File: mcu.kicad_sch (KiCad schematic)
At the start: 1 part, among them U1 XU316-1024-QF60A-C32

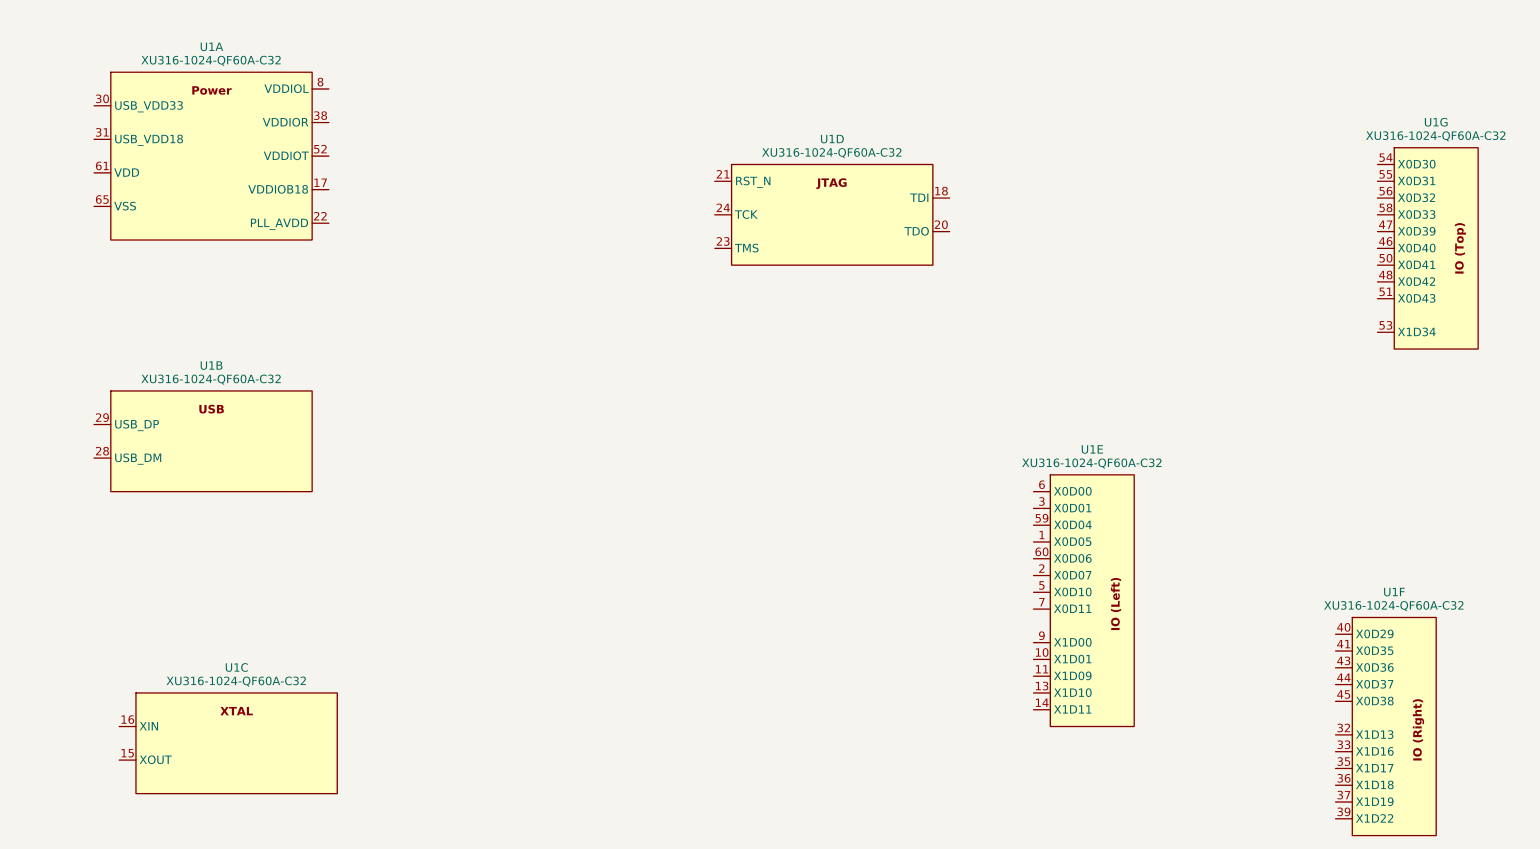
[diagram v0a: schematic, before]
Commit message: Began MCU schematic
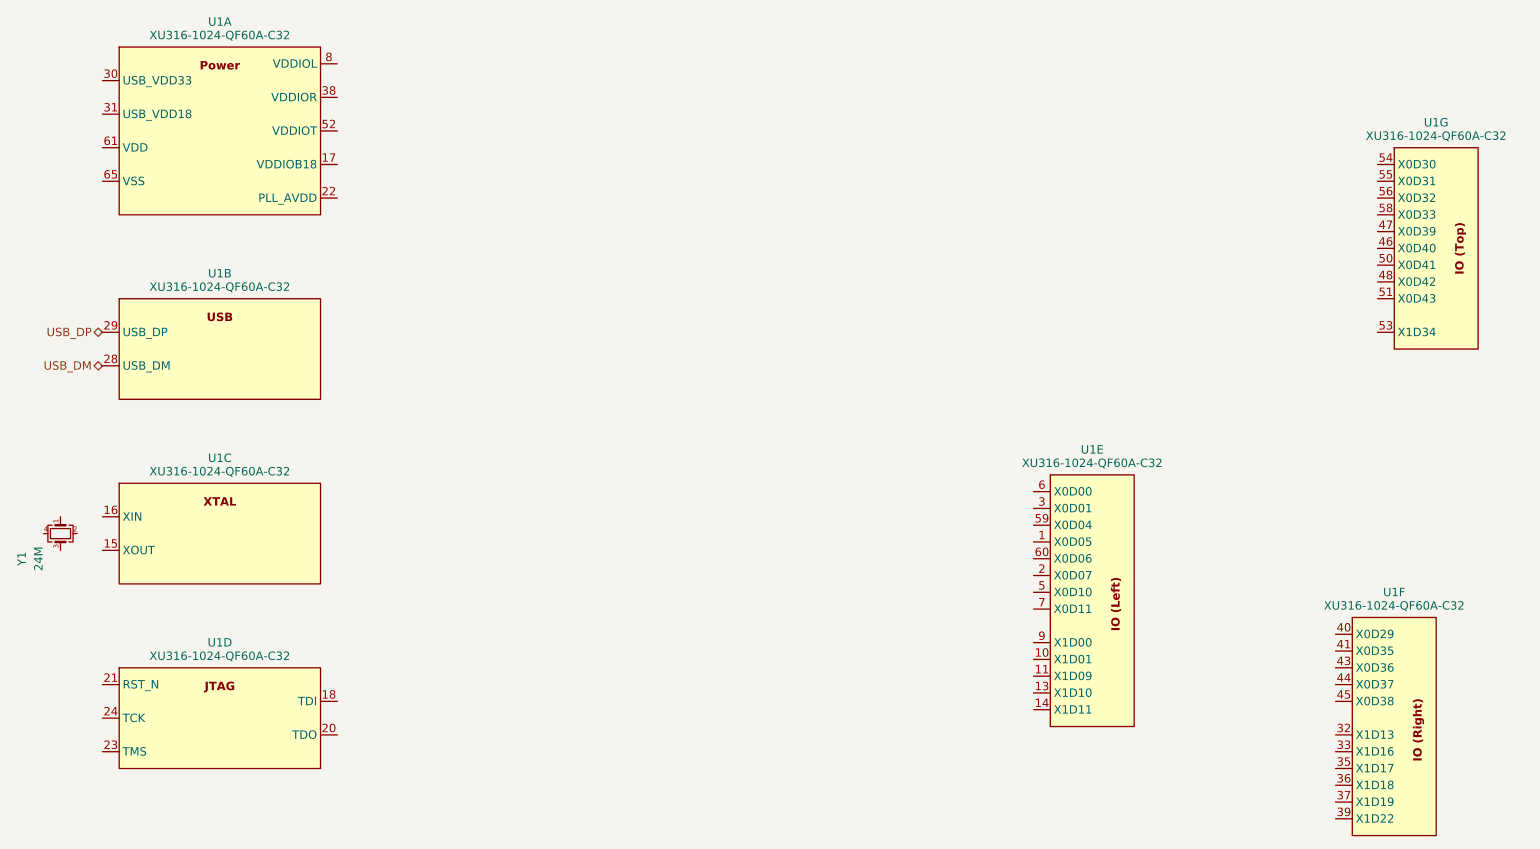
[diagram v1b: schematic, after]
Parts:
- added Y1: 24M, symbol Device:Crystal_GND24_Small
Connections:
- net USB_DM: now reaches U1.28 (USB_DM)
- net USB_DP: now reaches U1.29 (USB_DP)
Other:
- moved on the sheet: U1A, U1B, U1C, U1D
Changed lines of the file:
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@@
 	(generator_version "8.0")
 	(paper "A4")
+	(hierarchical_label "USB_DM"
+		(shape bidirectional)
+		(at 45.72 83.82 180)
+		(fields_autoplaced yes)
+		(effects
+			(font
+				(size 1.27 1.27)
+			)
+			(justify right)
+		)
+	)
+	(hierarchical_label "USB_DP"
+		(shape bidirectional)
+		(at 45.72 78.74 180)
+		(fields_autoplaced yes)
+		(effects
+			(font
+				(size 1.27 1.27)
+			)
+			(justify right)
+		)
+	)
 	(symbol
 		(lib_id "albert-custom:XU316-1024-QF60A-C32")
-		(at 62.23 83.82 0)
+		(at 63.5 69.85 0)
 		(unit 2)
 		(exclude_from_sim no)
@@
 		(fields_autoplaced yes)
 		(property "Reference" "U1"
-			(at 62.23 83.82 0)
+			(at 63.5 69.85 0)
 			(do_not_autoplace yes)
 			(effects
@@
 		)
 		(property "Value" "XU316-1024-QF60A-C32"
-			(at 62.23 85.852 0)
+			(at 63.5 71.882 0)
 			(do_not_autoplace yes)
 			(effects
@@
 		)
 		(property "Footprint" "lib_fp:XU316-1024-QF60A-C32_QFN-60_EP_7x7_Pitch0.4mm"
-			(at 62.23 83.82 0)
+			(at 63.5 69.85 0)
 			(effects
 				(font
@@
 		)
 		(property "Datasheet" "https://www.xmos.com/download/XU316-1024-QF60A-xcore.ai-Datasheet(22).pdf"
-			(at 62.23 83.82 0)
+			(at 63.5 69.85 0)
 			(effects
 				(font
@@
 		)
 		(property "Description" ""
-			(at 62.23 83.82 0)
+			(at 63.5 69.85 0)
 			(effects
 				(font
@@
 	(symbol
 		(lib_id "albert-custom:XU316-1024-QF60A-C32")
-		(at 66.04 129.54 0)
+		(at 63.5 97.79 0)
 		(unit 3)
 		(exclude_from_sim no)
@@
 		(fields_autoplaced yes)
 		(property "Reference" "U1"
-			(at 66.04 129.54 0)
+			(at 63.5 97.79 0)
 			(do_not_autoplace yes)
 			(effects
@@
 		)
 		(property "Value" "XU316-1024-QF60A-C32"
-			(at 66.04 131.572 0)
+			(at 63.5 99.822 0)
 			(do_not_autoplace yes)
 			(effects
@@
 		)
 		(property "Footprint" "lib_fp:XU316-1024-QF60A-C32_QFN-60_EP_7x7_Pitch0.4mm"
-			(at 66.04 129.54 0)
+			(at 63.5 97.79 0)
 			(effects
 				(font
@@
 		)
 		(property "Datasheet" "https://www.xmos.com/download/XU316-1024-QF60A-xcore.ai-Datasheet(22).pdf"
-			(at 66.04 129.54 0)
+			(at 63.5 97.79 0)
 			(effects
 				(font
@@
 		)
 		(property "Description" ""
-			(at 66.04 129.54 0)
+			(at 63.5 97.79 0)
 			(effects
 				(font
@@
 	)
 	(symbol
+		(lib_id "Device:Crystal_GND24_Small")
+		(at 39.37 109.22 90)
+		(mirror x)
+		(unit 1)
+		(exclude_from_sim no)
+		(in_bom yes)
+		(on_board yes)
+		(dnp no)
+		(property "Reference" "Y1"
+			(at 33.528 113.03 0)
+			(effects
+				(font
+					(size 1.27 1.27)
+				)
+			)
+		)
+		(property "Value" "24M"
+			(at 36.068 113.03 0)
+			(effects
+				(font
+					(size 1.27 1.27)
+				)
+			)
+		)
+		(property "Footprint" ""
+			(at 39.37 109.22 0)
+			(effects
+				(font
+					(size 1.27 1.27)
+				)
+				(hide yes)
+			)
+		)
+		(property "Datasheet" "~"
+			(at 39.37 109.22 0)
+			(effects
+				(font
+					(size 1.27 1.27)
+				)
+				(hide yes)
+			)
+		)
+		(property "Description" "Four pin crystal, GND on pins 2 and 4, small symbol"
+			(at 39.37 109.22 0)
+			(effects
+				(font
+					(size 1.27 1.27)
+				)
+				(hide yes)
+			)
+		)
+		(pin "1"
+		)
+		(pin "2"
+		)
+		(pin "3"
+		)
+		(pin "4"
+		)
+		(instances
+			(project ""
+				(path "/b16dfd04-6bfc-4d2d-ba2c-9a843d57dfb1/9717bff4-43fd-4c4d-9ccb-a8f356b7f1f3"
+					(reference "Y1")
+					(unit 1)
+				)
+			)
+		)
+	)
+	(symbol
 		(lib_id "albert-custom:XU316-1024-QF60A-C32")
-		(at 62.23 35.56 0)
+		(at 63.5 31.75 0)
 		(unit 1)
 		(exclude_from_sim no)
@@
 		(fields_autoplaced yes)
 		(property "Reference" "U1"
-			(at 62.23 35.56 0)
+			(at 63.5 31.75 0)
 			(do_not_autoplace yes)
 			(effects
@@
 		)
 		(property "Value" "XU316-1024-QF60A-C32"
-			(at 62.23 37.592 0)
+			(at 63.5 33.782 0)
 			(do_not_autoplace yes)
 			(effects
@@
 		)
 		(property "Footprint" "lib_fp:XU316-1024-QF60A-C32_QFN-60_EP_7x7_Pitch0.4mm"
-			(at 62.23 35.56 0)
+			(at 63.5 31.75 0)
 			(effects
 				(font
@@
 		)
 		(property "Datasheet" "https://www.xmos.com/download/XU316-1024-QF60A-xcore.ai-Datasheet(22).pdf"
-			(at 62.23 35.56 0)
+			(at 63.5 31.75 0)
 			(effects
 				(font
@@
 		)
 		(property "Description" ""
-			(at 62.23 35.56 0)
+			(at 63.5 31.75 0)
 			(effects
 				(font
@@
 	(symbol
 		(lib_id "albert-custom:XU316-1024-QF60A-C32")
-		(at 156.21 49.53 0)
+		(at 63.5 125.73 0)
 		(unit 4)
 		(exclude_from_sim no)
@@
 		(fields_autoplaced yes)
 		(property "Reference" "U1"
-			(at 156.21 49.53 0)
+			(at 63.5 125.73 0)
 			(do_not_autoplace yes)
 			(effects
@@
 		)
 		(property "Value" "XU316-1024-QF60A-C32"
-			(at 156.21 51.562 0)
+			(at 63.5 127.762 0)
 			(do_not_autoplace yes)
 			(effects
@@
 		)
 		(property "Footprint" "lib_fp:XU316-1024-QF60A-C32_QFN-60_EP_7x7_Pitch0.4mm"
-			(at 156.21 49.53 0)
+			(at 63.5 125.73 0)
 			(effects
 				(font
@@
 		)
 		(property "Datasheet" "https://www.xmos.com/download/XU316-1024-QF60A-xcore.ai-Datasheet(22).pdf"
-			(at 156.21 49.53 0)
+			(at 63.5 125.73 0)
 			(effects
 				(font
@@
 		)
 		(property "Description" ""
-			(at 156.21 49.53 0)
-			(effects
-				(font
+			(at 63.5 125.73 0)
+			(effects
+				(font
